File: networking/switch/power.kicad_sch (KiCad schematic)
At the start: 8 parts, among them J1 DC IN, U1 AP2112K-3.3

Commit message: Feat[switch]: added sheet metadata and magnetics symbols to sch
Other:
- company: (none) -> MUREX Robotics [Byran Huang and Max Liu]
- title: (none) -> MUREX Ethernet Switch (needs a better name)
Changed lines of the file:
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@@
 (kicad_sch (version 20230409) (generator eeschema)
   (paper "A4")
+  (title_block
+    (title "MUREX Ethernet Switch (needs a better name)")
+    (date "2023-08-30")
+    (rev "V1.0")
+    (company "MUREX Robotics [Byran Huang and Max Liu]")
+    (comment 3 "// INNOVATION FOR ALL.")
+    (comment 4 "// ATTEMPT THE IMPOSSIBLE.")
+  )
   (junction (at 130.81 101.6) (diameter 0) (color 0 0 0 0)
   )

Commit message: Feat[switch]: unpolished schematic complete
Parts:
- removed C2: 22uF, symbol Device:C_Small
- removed C5: 10uF, symbol Device:C_Small
- removed L1: 60Ω @ 100MHz/2A, symbol Device:L_Small
- removed U1: AP2112K-3.3, Package_TO_SOT_SMD:SOT-23-5, symbol Regulator_Linear:AP2112K-3.3
- added C2: 10uF, symbol Device:C_Polarized_Small
- added J7: 3.3V IN, symbol Connector_Generic:Conn_01x02
- added U5: LM1117MP-3.3, Package_TO_SOT_SMD:SOT-223-3_TabPin2, symbol Regulator_Linear:LM1117MP-3.3
- C1: value 47uF -> 10uF
- C3: value 1uF -> 0.1uF
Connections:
- net +3.3V: now also C1.1, C4.1, J7.1 (Pin_1), U5.2 (VO)
- net at J1.1: now also C3.1, C2.1, U5.3 (VI)
- net GND: now reaches C1.2, C3.2, C4.2, J1.2
- net GND: now also C2.2, J7.2 (Pin_2), U5.1 (GND)
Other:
- note added: "Direct 3.3V input"
- note added: "Fixed 3.3V output for up to 12V input, should be adequetely cooled with thermal vias"
- note added: "Tantalum capacitors for frequency rejection, see https://electronics.stackexchange.com/q/172447"
- note removed: "@TODO: change LDO selection"
- moved on the sheet: J1

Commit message: Feat[switch]: refactored schematic complete
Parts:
- added J8: LDO IN, symbol Connector_Generic:Conn_01x02
- renumbered C2 to C1, C3 to C2, C1 to C3, J7 to J2, U5 to U1
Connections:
- net GND: now also J8.1 (Pin_1)
- net at C1.1, C2.1, J1.1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: now also J8.2 (Pin_2)
- net +3.3V renamed VCC
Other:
- title: MUREX Ethernet Switch (needs a better name) -> MUREX Ethernet Switch
- moved on the sheet: J2

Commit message: Feat[switch]: created all necessary symbols and footprints, started PCB
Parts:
- C1, C2, C3, C4: footprint (none) -> Capacitor_SMD:C_0402_1005Metric
- J1: footprint (none) -> Connector_BarrelJack:BarrelJack_CUI_PJ-063AH_Horizontal
- J2, J8: footprint (none) -> Connector_Molex:Molex_PicoBlade_53398-0271_1x02-1MP_P1.25mm_Vertical
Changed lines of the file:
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@@
       (effects (font (size 1.27 1.27)))
     )
-    (property "Footprint" "" (at 114.3 114.046 0)
+    (property "Footprint" "Connector_BarrelJack:BarrelJack_CUI_PJ-063AH_Horizontal" (at 114.3 114.046 0)
       (effects (font (size 1.27 1.27)) hide)
     )
@@
       (effects (font (size 1.27 1.27)))
     )
-    (property "Footprint" "" (at 99.06 114.3 0)
+    (property "Footprint" "Connector_Molex:Molex_PicoBlade_53398-0271_1x02-1MP_P1.25mm_Vertical" (at 99.06 114.3 0)
       (effects (font (size 1.27 1.27)) hide)
     )
@@
       (effects (font (size 1.27 1.27)) (justify left))
     )
-    (property "Footprint" "" (at 171.45 113.03 0)
+    (property "Footprint" "Capacitor_SMD:C_0402_1005Metric" (at 171.45 113.03 0)
       (effects (font (size 1.27 1.27)) hide)
     )
@@
       (effects (font (size 1.27 1.27)) (justify left))
     )
-    (property "Footprint" "" (at 165.1 113.03 0)
+    (property "Footprint" "Capacitor_SMD:C_0402_1005Metric" (at 165.1 113.03 0)
       (effects (font (size 1.27 1.27)) hide)
     )
@@
       (effects (font (size 1.27 1.27)) (justify left))
     )
-    (property "Footprint" "" (at 137.16 113.03 0)
+    (property "Footprint" "Capacitor_SMD:C_0402_1005Metric" (at 137.16 113.03 0)
       (effects (font (size 1.27 1.27)) hide)
     )
@@
       (effects (font (size 1.27 1.27)) (justify left))
     )
-    (property "Footprint" "" (at 191.77 111.76 0)
+    (property "Footprint" "Connector_Molex:Molex_PicoBlade_53398-0271_1x02-1MP_P1.25mm_Vertical" (at 191.77 111.76 0)
       (effects (font (size 1.27 1.27)) hide)
     )
@@
       (effects (font (size 1.27 1.27)) (justify left))
     )
-    (property "Footprint" "" (at 127 113.03 0)
-      (effects (font (size 1.27 1.27)) hide)
-    )
+    (property "Footprint" "Capacitor_SMD:C_0402_1005Metric" (at 127 113.03 0)
+      (effects (font (size 1.27 1.27)) hide)
+    )

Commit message: Feat[switch]: initial board layout (FOLLOW @TODOs)
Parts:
- removed J1: DC IN, Connector_BarrelJack:BarrelJack_CUI_PJ-063AH_Horizontal, symbol Connector:Barrel_Jack
- C1, C3: footprint Capacitor_SMD:C_0402_1005Metric -> Capacitor_Tantalum_SMD:CP_EIA-3216-18_Kemet-A
- J1: renamed from J8; footprint Connector_Molex:Molex_PicoBlade_53398-0271_1x02-1MP_P1.25mm_Vertical -> Connector_Molex:Molex_PicoBlade_53047-0210_1x02_P1.25mm_Vertical
- J3: renamed from J2; footprint Connector_Molex:Molex_PicoBlade_53398-0271_1x02-1MP_P1.25mm_Vertical -> Connector_Molex:Molex_PicoBlade_53047-0210_1x02_P1.25mm_Vertical
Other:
- moved on the sheet: J1
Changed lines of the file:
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@@
   (junction (at 152.4 118.11) (diameter 0) (color 0 0 0 0)
   )
-  (junction (at 120.65 107.95) (diameter 0) (color 0 0 0 0)
-  )
   (junction (at 127 107.95) (diameter 0) (color 0 0 0 0)
   )
@@
   (junction (at 137.16 118.11) (diameter 0) (color 0 0 0 0)
   )
-  (junction (at 120.65 118.11) (diameter 0) (color 0 0 0 0)
-  )
   (wire (pts (xy 137.16 107.95) (xy 144.78 107.95))
     (stroke (width 0) (type default))
@@
     (stroke (width 0) (type default))
   )
-  (wire (pts (xy 120.65 118.11) (xy 127 118.11))
-    (stroke (width 0) (type default))
-  )
-  (wire (pts (xy 104.14 114.3) (xy 104.14 118.11))
+  (wire (pts (xy 116.84 114.3) (xy 116.84 118.11))
     (stroke (width 0) (type default))
   )
@@
     (stroke (width 0) (type default))
   )
-  (wire (pts (xy 120.65 107.95) (xy 120.65 110.49))
-    (stroke (width 0) (type default))
-  )
   (wire (pts (xy 152.4 115.57) (xy 152.4 118.11))
     (stroke (width 0) (type default))
@@
     (stroke (width 0) (type default))
   )
-  (wire (pts (xy 104.14 107.95) (xy 120.65 107.95))
-    (stroke (width 0) (type default))
-  )
   (wire (pts (xy 127 107.95) (xy 127 110.49))
     (stroke (width 0) (type default))
   )
-  (wire (pts (xy 120.65 115.57) (xy 120.65 118.11))
-    (stroke (width 0) (type default))
-  )
   (wire (pts (xy 137.16 115.57) (xy 137.16 118.11))
     (stroke (width 0) (type default))
   )
-  (wire (pts (xy 104.14 118.11) (xy 120.65 118.11))
+  (wire (pts (xy 116.84 118.11) (xy 127 118.11))
     (stroke (width 0) (type default))
   )
@@
     (stroke (width 0) (type default))
   )
-  (wire (pts (xy 104.14 111.76) (xy 104.14 107.95))
+  (wire (pts (xy 116.84 111.76) (xy 116.84 107.95))
     (stroke (width 0) (type default))
   )
@@
     (stroke (width 0) (type default))
   )
-  (wire (pts (xy 120.65 107.95) (xy 127 107.95))
+  (wire (pts (xy 116.84 107.95) (xy 127 107.95))
     (stroke (width 0) (type default))
   )
@@
     (effects (font (size 1.27 1.27)) (justify left bottom))
   )
-  (symbol (lib_id "Connector:Barrel_Jack") (at 113.03 113.03 0) (unit 1)
-    (in_bom yes) (on_board yes) (dnp no)
-    (property "Reference" "J1" (at 113.03 104.14 0)
-      (effects (font (size 1.27 1.27)))
-    )
-    (property "Value" "DC IN" (at 113.03 106.68 0)
-      (effects (font (size 1.27 1.27)))
-    )
-    (property "Footprint" "Connector_BarrelJack:BarrelJack_CUI_PJ-063AH_Horizontal" (at 114.3 114.046 0)
-      (effects (font (size 1.27 1.27)) hide)
-    )
-    (property "Datasheet" "~" (at 114.3 114.046 0)
+  (symbol (lib_id "Connector_Generic:Conn_01x02") (at 111.76 114.3 180) (unit 1)
+    (in_bom yes) (on_board yes) (dnp no) (fields_autoplaced)
+    (property "Reference" "J1" (at 111.76 106.68 0)
+      (effects (font (size 1.27 1.27)))
+    )
+    (property "Value" "LDO IN" (at 111.76 109.22 0)
+      (effects (font (size 1.27 1.27)))
+    )
+    (property "Footprint" "Connector_Molex:Molex_PicoBlade_53047-0210_1x02_P1.25mm_Vertical" (at 111.76 114.3 0)
+      (effects (font (size 1.27 1.27)) hide)
+    )
+    (property "Datasheet" "~" (at 111.76 114.3 0)
       (effects (font (size 1.27 1.27)) hide)
     )
@@
         (path "/3a8c8799-9295-4740-b990-f123ec1feb18/ae30af2c-3015-4dad-a9da-cdbd35ec9eec"
           (reference "J1") (unit 1)
-        )
-        (path "/3a8c8799-9295-4740-b990-f123ec1feb18/3b4e3a24-52bc-4456-b8ba-0ef7b116b867"
-          (reference "J2") (unit 1)
-        )
-      )
-    )
-  )
-  (symbol (lib_id "Connector_Generic:Conn_01x02") (at 99.06 114.3 180) (unit 1)
-    (in_bom yes) (on_board yes) (dnp no) (fields_autoplaced)
-    (property "Reference" "J8" (at 99.06 106.68 0)
-      (effects (font (size 1.27 1.27)))
-    )
-    (property "Value" "LDO IN" (at 99.06 109.22 0)
-      (effects (font (size 1.27 1.27)))
-    )
-    (property "Footprint" "Connector_Molex:Molex_PicoBlade_53398-0271_1x02-1MP_P1.25mm_Vertical" (at 99.06 114.3 0)
-      (effects (font (size 1.27 1.27)) hide)
-    )
-    (property "Datasheet" "~" (at 99.06 114.3 0)
-      (effects (font (size 1.27 1.27)) hide)
-    )
-    (pin "1")
-    (pin "2")
-    (instances
-      (project "switch"
-        (path "/3a8c8799-9295-4740-b990-f123ec1feb18/ae30af2c-3015-4dad-a9da-cdbd35ec9eec"
-          (reference "J8") (unit 1)
         )
       )
@@
       (effects (font (size 1.27 1.27)) (justify left))
     )
-    (property "Footprint" "Capacitor_SMD:C_0402_1005Metric" (at 165.1 113.03 0)
+    (property "Footprint" "Capacitor_Tantalum_SMD:CP_EIA-3216-18_Kemet-A" (at 165.1 113.03 0)
       (effects (font (size 1.27 1.27)) hide)
     )
@@
   (symbol (lib_id "Connector_Generic:Conn_01x02") (at 191.77 111.76 0) (unit 1)
     (in_bom yes) (on_board yes) (dnp no) (fields_autoplaced)
-    (property "Reference" "J2" (at 194.31 112.395 0)
+    (property "Reference" "J3" (at 194.31 112.395 0)
       (effects (font (size 1.27 1.27)) (justify left))
     )
@@
       (effects (font (size 1.27 1.27)) (justify left))
     )
-    (property "Footprint" "Connector_Molex:Molex_PicoBlade_53398-0271_1x02-1MP_P1.25mm_Vertical" (at 191.77 111.76 0)
+    (property "Footprint" "Connector_Molex:Molex_PicoBlade_53047-0210_1x02_P1.25mm_Vertical" (at 191.77 111.76 0)
       (effects (font (size 1.27 1.27)) hide)
     )
@@
       (project "switch"
         (path "/3a8c8799-9295-4740-b990-f123ec1feb18/ae30af2c-3015-4dad-a9da-cdbd35ec9eec"
-          (reference "J2") (unit 1)
+          (reference "J3") (unit 1)
         )
       )
@@
       (effects (font (size 1.27 1.27)) (justify left))
     )
-    (property "Footprint" "Capacitor_SMD:C_0402_1005Metric" (at 127 113.03 0)
-      (effects (font (size 1.27 1.27)) hide)
-    )
+    (property "Footprint" "Capacitor_Tantalum_SMD:CP_EIA-3216-18_Kemet-A" (at 127 113.03 0)
+      (effects (font (size 1.27 1.27)) hide)
+    )

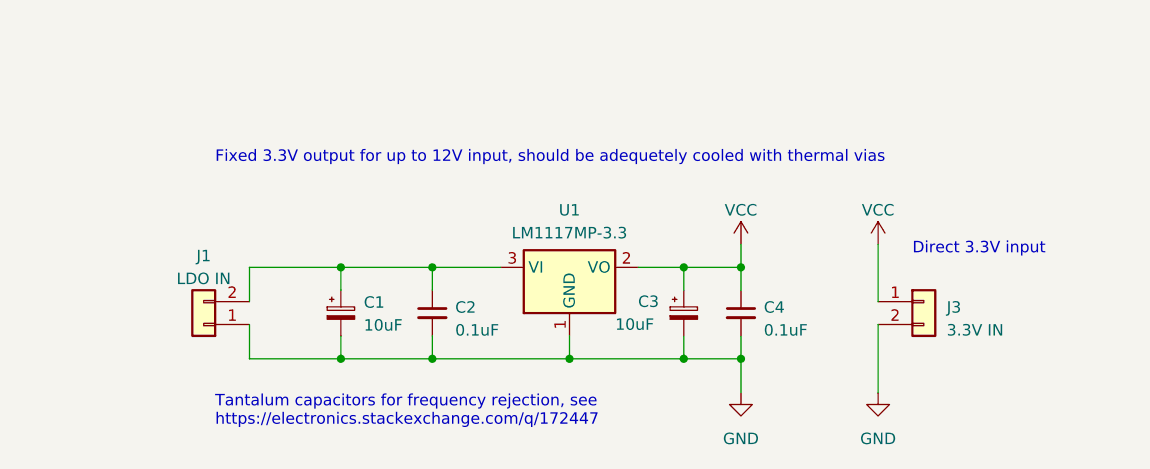
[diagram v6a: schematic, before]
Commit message: Feat[switch]: Added diode, initial silkscreen
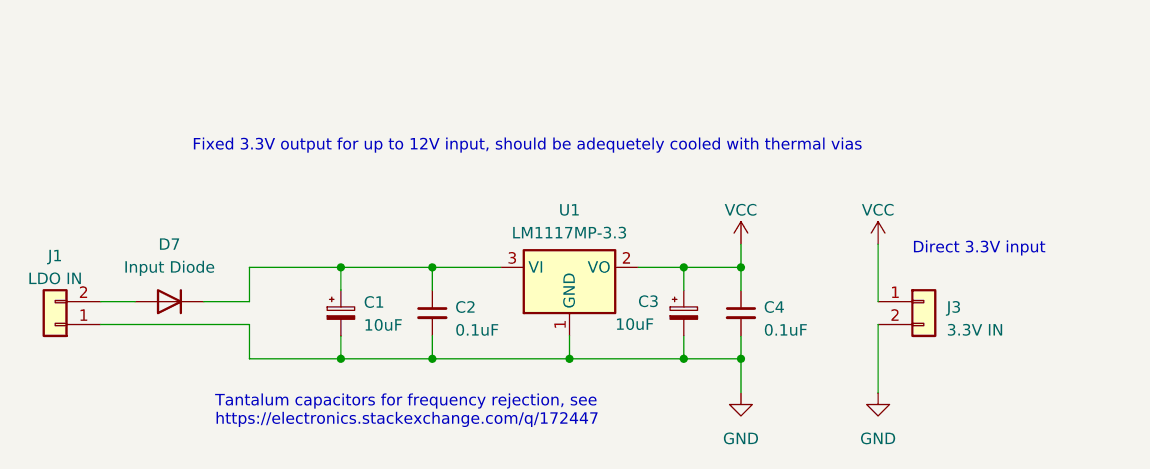
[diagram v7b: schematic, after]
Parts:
- added D7: Input Diode, Diode_SMD:D_SMA, symbol Device:D
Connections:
- net at C1.1, C2.1, U1.3 (VI): now also D7.1 (K); no longer J1.2 (Pin_2)
- new net: D7.2 (A), J1.2 (Pin_2)
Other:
- moved on the sheet: J1
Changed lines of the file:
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@@
-(kicad_sch (version 20230409) (generator eeschema)
+(kicad_sch (version 20230819) (generator eeschema)
   (paper "A4")
   (title_block
@@
     (stroke (width 0) (type default))
   )
+  (wire (pts (xy 100.33 114.3) (xy 116.84 114.3))
+    (stroke (width 0) (type default))
+  )
   (wire (pts (xy 116.84 114.3) (xy 116.84 118.11))
     (stroke (width 0) (type default))
@@
     (stroke (width 0) (type default))
   )
+  (wire (pts (xy 100.33 111.76) (xy 104.14 111.76))
+    (stroke (width 0) (type default))
+  )
   (wire (pts (xy 152.4 115.57) (xy 152.4 118.11))
     (stroke (width 0) (type default))
@@
   )
   (wire (pts (xy 171.45 105.41) (xy 171.45 107.95))
+    (stroke (width 0) (type default))
+  )
+  (wire (pts (xy 111.76 111.76) (xy 116.84 111.76))
     (stroke (width 0) (type default))
   )
@@
   )
   (text "Fixed 3.3V output for up to 12V input, should be adequetely cooled with thermal vias" (exclude_from_sim no)
-    (at 113.03 96.52 0)
+    (at 110.49 95.25 0)
     (effects (font (size 1.27 1.27)) (justify left bottom))
   )
-  (symbol (lib_id "Connector_Generic:Conn_01x02") (at 111.76 114.3 180) (unit 1)
-    (in_bom yes) (on_board yes) (dnp no) (fields_autoplaced)
-    (property "Reference" "J1" (at 111.76 106.68 0)
-      (effects (font (size 1.27 1.27)))
-    )
-    (property "Value" "LDO IN" (at 111.76 109.22 0)
-      (effects (font (size 1.27 1.27)))
-    )
-    (property "Footprint" "Connector_Molex:Molex_PicoBlade_53047-0210_1x02_P1.25mm_Vertical" (at 111.76 114.3 0)
-      (effects (font (size 1.27 1.27)) hide)
-    )
-    (property "Datasheet" "~" (at 111.76 114.3 0)
+  (symbol (lib_id "Connector_Generic:Conn_01x02") (at 95.25 114.3 180) (unit 1)
+    (exclude_from_sim no) (in_bom yes) (on_board yes) (dnp no) (fields_autoplaced)
+    (property "Reference" "J1" (at 95.25 106.68 0)
+      (effects (font (size 1.27 1.27)))
+    )
+    (property "Value" "LDO IN" (at 95.25 109.22 0)
+      (effects (font (size 1.27 1.27)))
+    )
+    (property "Footprint" "Connector_Molex:Molex_PicoBlade_53047-0210_1x02_P1.25mm_Vertical" (at 95.25 114.3 0)
+      (effects (font (size 1.27 1.27)) hide)
+    )
+    (property "Datasheet" "~" (at 95.25 114.3 0)
+      (effects (font (size 1.27 1.27)) hide)
+    )
+    (property "Description" "" (at 95.25 114.3 0)
       (effects (font (size 1.27 1.27)) hide)
     )
@@
   )
   (symbol (lib_id "power:VCC") (at 171.45 105.41 0) (unit 1)
-    (in_bom yes) (on_board yes) (dnp no) (fields_autoplaced)
+    (exclude_from_sim no) (in_bom yes) (on_board yes) (dnp no) (fields_autoplaced)
     (property "Reference" "#PWR03" (at 171.45 109.22 0)
       (effects (font (size 1.27 1.27)) hide)
@@
     )
     (property "Datasheet" "" (at 171.45 105.41 0)
+      (effects (font (size 1.27 1.27)) hide)
+    )
+    (property "Description" "" (at 171.45 105.41 0)
       (effects (font (size 1.27 1.27)) hide)
     )
@@
   )
   (symbol (lib_id "Regulator_Linear:LM1117MP-3.3") (at 152.4 107.95 0) (unit 1)
-    (in_bom yes) (on_board yes) (dnp no) (fields_autoplaced)
+    (exclude_from_sim no) (in_bom yes) (on_board yes) (dnp no) (fields_autoplaced)
     (property "Reference" "U1" (at 152.4 101.6 0)
       (effects (font (size 1.27 1.27)))
@@
       (effects (font (size 1.27 1.27)) hide)
     )
+    (property "Description" "" (at 152.4 107.95 0)
+      (effects (font (size 1.27 1.27)) hide)
+    )
     (pin "1")
     (pin "2")
@@
   )
   (symbol (lib_id "power:GND") (at 171.45 121.92 0) (unit 1)
-    (in_bom yes) (on_board yes) (dnp no) (fields_autoplaced)
+    (exclude_from_sim no) (in_bom yes) (on_board yes) (dnp no) (fields_autoplaced)
     (property "Reference" "#PWR02" (at 171.45 128.27 0)
       (effects (font (size 1.27 1.27)) hide)
@@
       (effects (font (size 1.27 1.27)) hide)
     )
+    (property "Description" "" (at 171.45 121.92 0)
+      (effects (font (size 1.27 1.27)) hide)
+    )
     (pin "1")
     (instances
@@
   )
   (symbol (lib_id "Device:C_Small") (at 171.45 113.03 0) (unit 1)
-    (in_bom yes) (on_board yes) (dnp no) (fields_autoplaced)
+    (exclude_from_sim no) (in_bom yes) (on_board yes) (dnp no) (fields_autoplaced)
     (property "Reference" "C4" (at 173.99 112.4013 0)
       (effects (font (size 1.27 1.27)) (justify left))
@@
       (effects (font (size 1.27 1.27)) hide)
     )
+    (property "Description" "" (at 171.45 113.03 0)
+      (effects (font (size 1.27 1.27)) hide)
+    )
     (pin "1")
     (pin "2")
@@
   )
   (symbol (lib_id "Device:C_Polarized_Small") (at 165.1 113.03 0) (unit 1)
-    (in_bom yes) (on_board yes) (dnp no)
+    (exclude_from_sim no) (in_bom yes) (on_board yes) (dnp no)
     (property "Reference" "C3" (at 160.02 111.76 0)
       (effects (font (size 1.27 1.27)) (justify left))
@@
       (effects (font (size 1.27 1.27)) hide)
     )
+    (property "Description" "" (at 165.1 113.03 0)
+      (effects (font (size 1.27 1.27)) hide)
+    )
     (pin "1")
     (pin "2")
@@
   )
   (symbol (lib_id "power:VCC") (at 186.69 105.41 0) (unit 1)
-    (in_bom yes) (on_board yes) (dnp no) (fields_autoplaced)
+    (exclude_from_sim no) (in_bom yes) (on_board yes) (dnp no) (fields_autoplaced)
     (property "Reference" "#PWR03" (at 186.69 109.22 0)
       (effects (font (size 1.27 1.27)) hide)
@@
     )
     (property "Datasheet" "" (at 186.69 105.41 0)
+      (effects (font (size 1.27 1.27)) hide)
+    )
+    (property "Description" "" (at 186.69 105.41 0)
       (effects (font (size 1.27 1.27)) hide)
     )
@@
   )
   (symbol (lib_id "Device:C_Small") (at 137.16 113.03 0) (unit 1)
-    (in_bom yes) (on_board yes) (dnp no) (fields_autoplaced)
+    (exclude_from_sim no) (in_bom yes) (on_board yes) (dnp no) (fields_autoplaced)
     (property "Reference" "C2" (at 139.7 112.4013 0)
       (effects (font (size 1.27 1.27)) (justify left))
@@
       (effects (font (size 1.27 1.27)) hide)
     )
+    (property "Description" "" (at 137.16 113.03 0)
+      (effects (font (size 1.27 1.27)) hide)
+    )
     (pin "1")
     (pin "2")
@@
   )
   (symbol (lib_id "Connector_Generic:Conn_01x02") (at 191.77 111.76 0) (unit 1)
-    (in_bom yes) (on_board yes) (dnp no) (fields_autoplaced)
+    (exclude_from_sim no) (in_bom yes) (on_board yes) (dnp no) (fields_autoplaced)
     (property "Reference" "J3" (at 194.31 112.395 0)
       (effects (font (size 1.27 1.27)) (justify left))
@@
       (effects (font (size 1.27 1.27)) hide)
     )
+    (property "Description" "" (at 191.77 111.76 0)
+      (effects (font (size 1.27 1.27)) hide)
+    )
     (pin "1")
     (pin "2")
@@
   )
   (symbol (lib_id "power:GND") (at 186.69 121.92 0) (unit 1)
-    (in_bom yes) (on_board yes) (dnp no) (fields_autoplaced)
+    (exclude_from_sim no) (in_bom yes) (on_board yes) (dnp no) (fields_autoplaced)
     (property "Reference" "#PWR04" (at 186.69 128.27 0)
       (effects (font (size 1.27 1.27)) hide)
@@
       (effects (font (size 1.27 1.27)) hide)
     )
+    (property "Description" "" (at 186.69 121.92 0)
+      (effects (font (size 1.27 1.27)) hide)
+    )
     (pin "1")
     (instances
@@
   )
   (symbol (lib_id "Device:C_Polarized_Small") (at 127 113.03 0) (unit 1)
-    (in_bom yes) (on_board yes) (dnp no) (fields_autoplaced)
+    (exclude_from_sim no) (in_bom yes) (on_board yes) (dnp no) (fields_autoplaced)
     (property "Reference" "C1" (at 129.54 111.8489 0)
       (effects (font (size 1.27 1.27)) (justify left))
@@
       (effects (font (size 1.27 1.27)) hide)
     )
+    (property "Description" "" (at 127 113.03 0)
+      (effects (font (size 1.27 1.27)) hide)
+    )
     (pin "1")
     (pin "2")
@@
         )
       )
+    )
+  )
+  (symbol (lib_id "Device:D") (at 107.95 111.76 180) (unit 1)
+    (exclude_from_sim no) (in_bom yes) (on_board yes) (dnp no) (fields_autoplaced)
+    (property "Reference" "D7" (at 107.95 105.41 0)
+      (effects (font (size 1.27 1.27)))
+    )
+    (property "Value" "Input Diode" (at 107.95 107.95 0)
+      (effects (font (size 1.27 1.27)))
+    )
+    (property "Footprint" "Diode_SMD:D_SMA" (at 107.95 111.76 0)
+      (effects (font (size 1.27 1.27)) hide)
+    )
+    (property "Datasheet" "~" (at 107.95 111.76 0)
+      (effects (font (size 1.27 1.27)) hide)
+    )
+    (property "Description" "Diode" (at 107.95 111.76 0)
+      (effects (font (size 1.27 1.27)) hide)
+    )
+    (property "Sim.Device" "D" (at 107.95 111.76 0)
+      (effects (font (size 1.27 1.27)) hide)
+    )
+    (property "Sim.Pins" "1=K 2=A" (at 107.95 111.76 0)
+      (effects (font (size 1.27 1.27)) hide)
+    )
+    (pin "2")
+    (pin "1")
+    (instances
+      (project "switch"
+        (path "/3a8c8799-9295-4740-b990-f123ec1feb18/ae30af2c-3015-4dad-a9da-cdbd35ec9eec"
+          (reference "D7") (unit 1)
+        )
+      )
